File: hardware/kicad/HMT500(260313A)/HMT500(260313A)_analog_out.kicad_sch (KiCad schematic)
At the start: 30 parts, among them U10 TPS26611DDFR, U12 OPA197IDBVR, U13 OPA197IDBVR, U14 SN74LVC2G32DCUR, U7 DAC8760IPWP, U8 DAC8760IPWP, U9 TPS26611DDFR

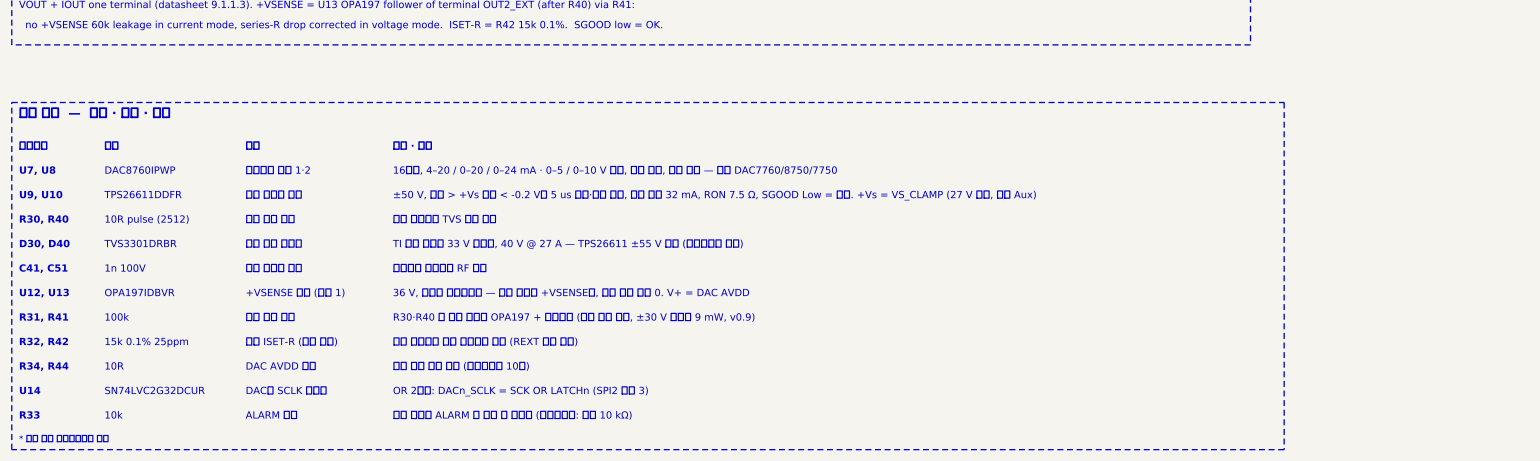
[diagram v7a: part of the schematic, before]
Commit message: Apply agreed external review items (decision #35)
- H01: series 100 V Schottky D3 (PMEG10010ELR) between D2 and eFuse IN
  (new net VIN_D) so negative surges no longer stress U1 IN-OUT
- H02: RS-485 bus TVS D60/D61 (TVS3301); U11 -> THVD2410DGKR (VSSOP-8)
- H04: +Vs clamp zener 27 V -> 24 V (BZX84C24LT1G)
- H08: ADS1220 IDAC fixed at 250 uA
- Room for new parts: C7 removed, 37 low-voltage R/C moved to 0402
  (LCSC basic where available); chassis parts keep CH_GAP between each other
- Placement 104/104, netlist 78/78, pcbnew DRC: no clearance errors,
  assembly sim 23 OK; parts list / JLC BOM updated
- docs/hw/external-review-response-260930.md: item responses, output load
  table, current budget, firmware requirements F1-F6, tests T1-T7

Co-Authored-By: Claude Opus 5.5 <noreply@anthropic.com>
Claude-Session: https://claude.ai/code/session_01JA2o8uJsqp9Vzsg4b665ev
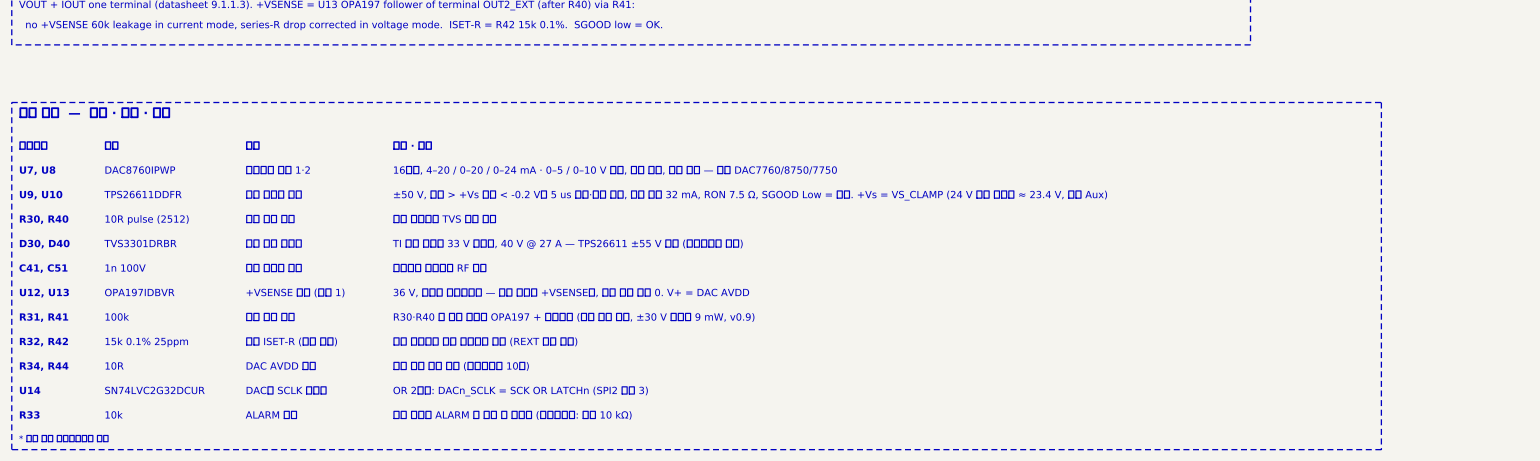
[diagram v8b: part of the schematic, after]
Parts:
- C36, C40, C44, C50, C54: footprint Capacitor_SMD:C_0603_1608Metric -> Capacitor_SMD:C_0402_1005Metric
- R31, R33, R34, R41, R44: footprint Resistor_SMD:R_0603_1608Metric -> Resistor_SMD:R_0402_1005Metric
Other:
- note added: "±50 V, 단자 > +Vs 또는 < -0.2 V면 5 us 차단·자동 복귀, 전류 제한 32 mA, RON 7.5 Ω, SGOOD Low = 정상. +Vs = VS_CLAMP (24 V 제너 폴로워 ≈ 23.4 V, 시트 Aux)"
- note removed: "±50 V, 단자 > +Vs 또는 < -0.2 V면 5 us 차단·자동 복귀, 전류 제한 32 mA, RON 7.5 Ω, SGOOD Low = 정상. +Vs = VS_CLAMP (27 V 제너, 시트 Aux)"
